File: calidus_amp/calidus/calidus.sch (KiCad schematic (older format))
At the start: 0 parts

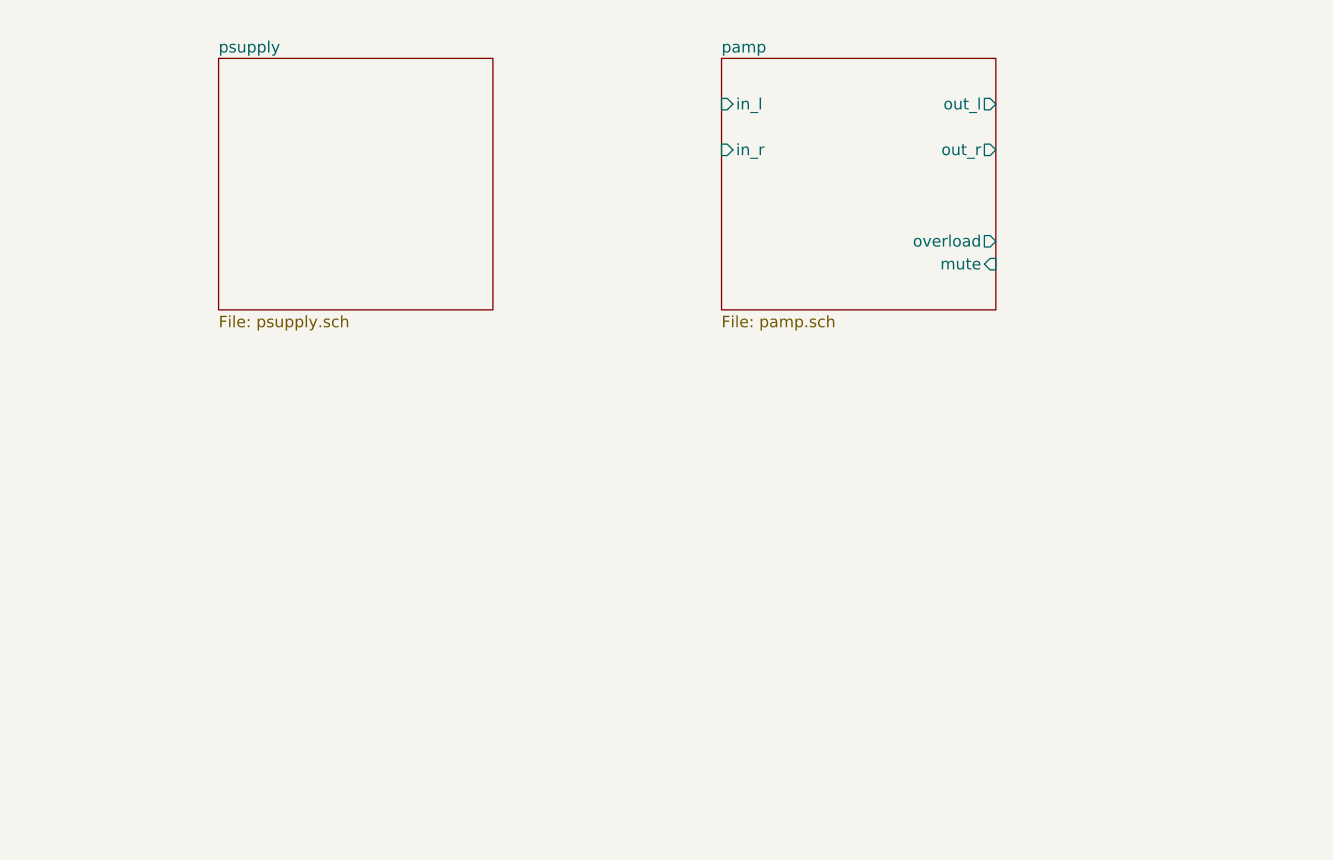
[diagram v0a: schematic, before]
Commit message: Update of the schematic
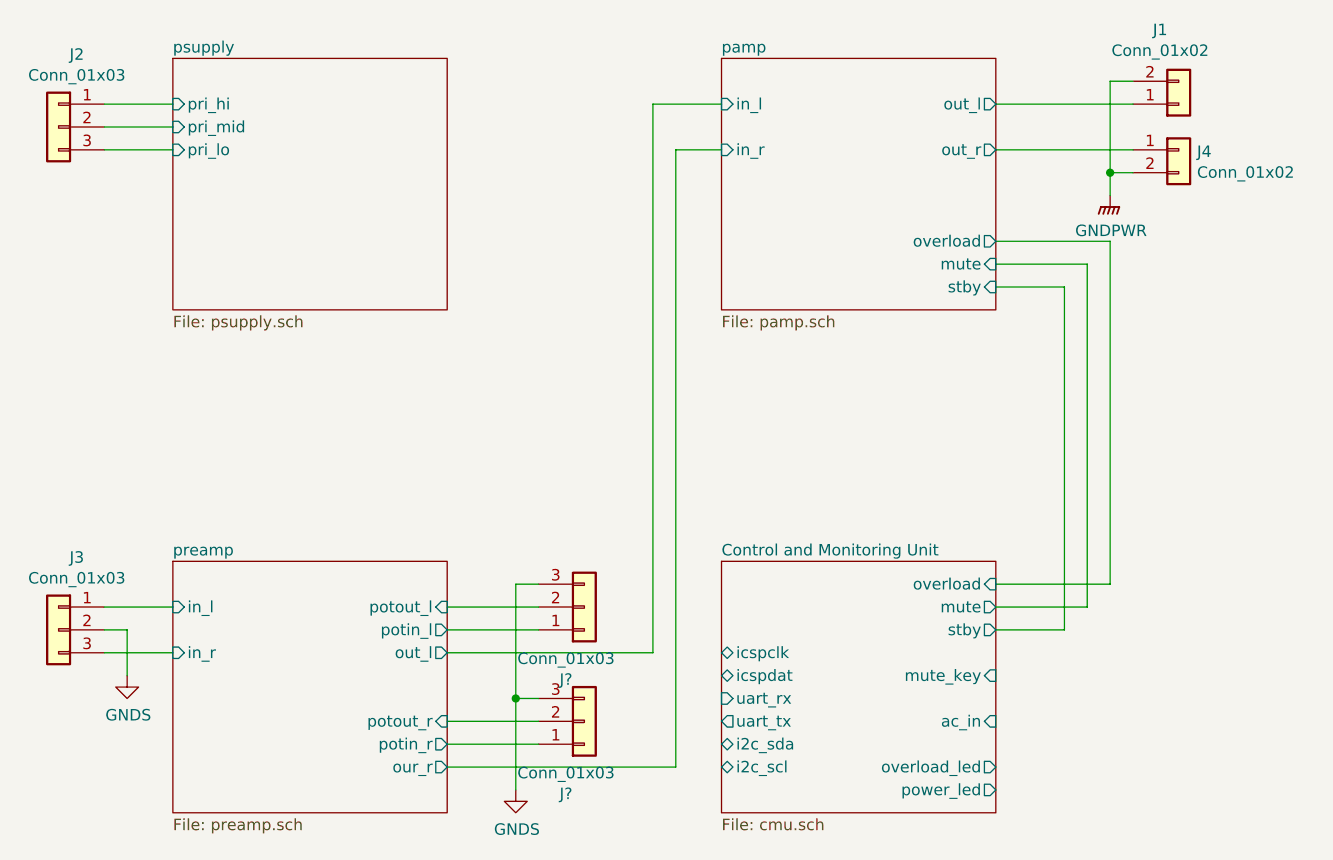
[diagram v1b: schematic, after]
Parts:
- added J1, J4: Conn_01x02, symbol Connector_Generic:Conn_01x02
- added J2, J3, J? (x2): Conn_01x03, symbol Connector_Generic:Conn_01x03
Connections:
- net pamp/out_l: now also J1.1 (Pin_1)
- net pamp/out_r: now also J4.1 (Pin_1)
- new net GNDPWR: J1.2 (Pin_2), J4.2 (Pin_2)
- new net GNDS: J3.2 (Pin_2), J?.3 (Pin_3), J?.3 (Pin_3)
- new net preamp/in_l: J3.1 (Pin_1)
- new net preamp/in_r: J3.3 (Pin_3)
- new net preamp/potin_l: J?.1 (Pin_1)
- new net preamp/potin_r: J?.1 (Pin_1)
- new net preamp/potout_l: J?.2 (Pin_2)
- new net preamp/potout_r: J?.2 (Pin_2)
- new net psupply/pri_hi: J2.1 (Pin_1)
- new net psupply/pri_lo: J2.3 (Pin_3)
- new net psupply/pri_mid: J2.2 (Pin_2)
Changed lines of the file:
@@
 $Descr A4 11693 8268
 encoding utf-8
-Sheet 1 3
+Sheet 1 5
 Title ""
 Date ""
@@
 $EndDescr
 $Sheet
-S 2100 1600 1200 1100
+S 1900 1600 1200 1100
 U 5C37BC48
 F0 "psupply" 50
 F1 "psupply.sch" 50
+F2 "pri_hi" I L 1900 1800 50
+F3 "pri_mid" I L 1900 1900 50
+F4 "pri_lo" I L 1900 2000 50
 $EndSheet
 $Sheet
@@
 F6 "in_r" I L 4300 2000 50
 F7 "out_r" O R 5500 2000 50
-$EndSheet
+F8 "stby" I R 5500 2600 50
+$EndSheet
+$Comp
+L Connector_Generic:Conn_01x03 J2
+U 1 1 5C47FAB8
+P 1400 1900
+F 0 "J2" H 1320 2217 50  0000 C CNN
+F 1 "Conn_01x03" H 1320 2126 50  0000 C CNN
+F 2 "" H 1400 1900 50  0001 C CNN
+F 3 "~" H 1400 1900 50  0001 C CNN
+	1    1400 1900
+	-1   0    0    -1
+$EndComp
+Wire Wire Line
+	1600 1800 1900 1800
+Wire Wire Line
+	1600 1900 1900 1900
+Wire Wire Line
+	1600 2000 1900 2000
+$Comp
+L Connector_Generic:Conn_01x03 J3
+U 1 1 5C47FB17
+P 1400 4100
+F 0 "J3" H 1320 4417 50  0000 C CNN
+F 1 "Conn_01x03" H 1320 4326 50  0000 C CNN
+F 2 "" H 1400 4100 50  0001 C CNN
+F 3 "~" H 1400 4100 50  0001 C CNN
+	1    1400 4100
+	-1   0    0    -1
+$EndComp
+$Comp
+L power:GNDS #PWR01
+U 1 1 5C47FB54
+P 1700 4300
+F 0 "#PWR01" H 1700 4050 50  0001 C CNN
+F 1 "GNDS" H 1705 4127 50  0000 C CNN
+F 2 "" H 1700 4300 50  0001 C CNN
+F 3 "" H 1700 4300 50  0001 C CNN
+	1    1700 4300
+	1    0    0    -1
+$EndComp
+Wire Wire Line
+	1700 4300 1700 4100
+Wire Wire Line
+	1700 4100 1600 4100
+Wire Wire Line
+	1600 4000 1900 4000
+Wire Wire Line
+	1600 4200 1900 4200
+$Comp
+L Connector_Generic:Conn_01x02 J1
+U 1 1 5C47FBF8
+P 6300 1800
+F 0 "J1" H 6219 1475 50  0000 C CNN
+F 1 "Conn_01x02" H 6219 1566 50  0000 C CNN
+F 2 "" H 6300 1800 50  0001 C CNN
+F 3 "~" H 6300 1800 50  0001 C CNN
+	1    6300 1800
+	1    0    0    1
+$EndComp
+$Comp
+L Connector_Generic:Conn_01x02 J4
+U 1 1 5C47FC30
+P 6300 2000
+F 0 "J4" H 6380 1992 50  0000 L CNN
+F 1 "Conn_01x02" H 6380 1901 50  0000 L CNN
+F 2 "" H 6300 2000 50  0001 C CNN
+F 3 "~" H 6300 2000 50  0001 C CNN
+	1    6300 2000
+	1    0    0    -1
+$EndComp
+Wire Wire Line
+	5500 1800 6100 1800
+Wire Wire Line
+	5500 2000 6100 2000
+Wire Wire Line
+	6100 1700 6000 1700
+Wire Wire Line
+	6000 1700 6000 2100
+Wire Wire Line
+	6000 2100 6100 2100
+$Comp
+L power:GNDPWR #PWR02
+U 1 1 5C47FEE1
+P 6000 2200
+F 0 "#PWR02" H 6000 2000 50  0001 C CNN
+F 1 "GNDPWR" H 6004 2046 50  0000 C CNN
+F 2 "" H 6000 2150 50  0001 C CNN
+F 3 "" H 6000 2150 50  0001 C CNN
+	1    6000 2200
+	1    0    0    -1
+$EndComp
+Wire Wire Line
+	6000 2200 6000 2100
+Connection ~ 6000 2100
+$Sheet
+S 1900 3800 1200 1100
+U 5C4751C0
+F0 "preamp" 50
+F1 "preamp.sch" 50
+F2 "potout_l" I R 3100 4000 50
+F3 "potin_l" O R 3100 4100 50
+F4 "out_l" O R 3100 4200 50
+F5 "in_l" I L 1900 4000 50
+F6 "in_r" I L 1900 4200 50
+F7 "potin_r" O R 3100 4600 50
+F8 "potout_r" I R 3100 4500 50
+F9 "our_r" O R 3100 4700 50
+$EndSheet
+Wire Wire Line
+	3100 4200 4000 4200
+Wire Wire Line
+	4000 4200 4000 1800
+Wire Wire Line
+	4000 1800 4300 1800
+Wire Wire Line
+	3100 4700 4100 4700
+Wire Wire Line
+	4100 4700 4100 2000
+Wire Wire Line
+	4100 2000 4300 2000
+$Comp
+L Connector_Generic:Conn_01x03 J?
+U 1 1 5C438B71
+P 3700 4000
+F 0 "J?" H 3620 4317 50  0000 C CNN
+F 1 "Conn_01x03" H 3620 4226 50  0000 C CNN
+F 2 "" H 3700 4000 50  0001 C CNN
+F 3 "~" H 3700 4000 50  0001 C CNN
+	1    3700 4000
+	1    0    0    1
+$EndComp
+Wire Wire Line
+	3100 4100 3500 4100
+Wire Wire Line
+	3500 4000 3100 4000
+$Comp
+L Connector_Generic:Conn_01x03 J?
+U 1 1 5C4396C1
+P 3700 4500
+F 0 "J?" H 3620 4817 50  0000 C CNN
+F 1 "Conn_01x03" H 3620 4726 50  0000 C CNN
+F 2 "" H 3700 4500 50  0001 C CNN
+F 3 "~" H 3700 4500 50  0001 C CNN
+	1    3700 4500
+	1    0    0    1
+$EndComp
+Wire Wire Line
+	3500 4600 3100 4600
+Wire Wire Line
+	3100 4500 3500 4500
+Wire Wire Line
+	3400 4800 3400 4400
+Wire Wire Line
+	3400 4400 3500 4400
+Wire Wire Line
+	3400 4400 3400 3900
+Wire Wire Line
+	3400 3900 3500 3900
+Connection ~ 3400 4400
+$Comp
+L power:GNDS #PWR?
+U 1 1 5C43A2D2
+P 3400 4800
+F 0 "#PWR?" H 3400 4550 50  0001 C CNN
+F 1 "GNDS" H 3405 4627 50  0000 C CNN
+F 2 "" H 3400 4800 50  0001 C CNN
+F 3 "" H 3400 4800 50  0001 C CNN
+	1    3400 4800
+	1    0    0    -1
+$EndComp
+$Sheet
+S 4300 3800 1200 1100
+U 5C43C4AB
+F0 "Control and Monitoring Unit" 50
+F1 "cmu.sch" 50
+F2 "mute" O R 5500 4000 50
+F3 "stby" O R 5500 4100 50
+F4 "power_led" O R 5500 4800 50
+F5 "overload_led" O R 5500 4700 50
+F6 "overload" I R 5500 3900 50
+F7 "ac_in" I R 5500 4500 50
+F8 "mute_key" I R 5500 4300 50
+F9 "icspclk" B L 4300 4200 50
+F10 "icspdat" B L 4300 4300 50
+F11 "uart_rx" I L 4300 4400 50
+F12 "uart_tx" O L 4300 4500 50
+F13 "i2c_sda" B L 4300 4600 50
+F14 "i2c_scl" B L 4300 4700 50
+$EndSheet
+Wire Wire Line
+	5500 2600 5800 2600
+Wire Wire Line
+	5800 2600 5800 4100
+Wire Wire Line
+	5800 4100 5500 4100
+Wire Wire Line
+	5500 4000 5900 4000
+Wire Wire Line
+	5900 4000 5900 2500
+Wire Wire Line
+	5900 2500 5500 2500
+Wire Wire Line
+	5500 2400 6000 2400
+Wire Wire Line
+	6000 2400 6000 3900
+Wire Wire Line
+	6000 3900 5500 3900
 $EndSCHEMATC

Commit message: Daily update
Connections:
- net preamp/potout_l is gone; now on net pamp/in_l: J?.2 (Pin_2)
- net preamp/potout_r is gone; now on net pamp/in_r: J?.2 (Pin_2)
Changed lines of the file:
@@
 F2 "potout_l" I R 3100 4000 50
 F3 "potin_l" O R 3100 4100 50
-F4 "out_l" O R 3100 4200 50
 F5 "in_l" I L 1900 4000 50
 F6 "in_r" I L 1900 4200 50
 F7 "potin_r" O R 3100 4600 50
 F8 "potout_r" I R 3100 4500 50
-F9 "our_r" O R 3100 4700 50
 $EndSheet
 Wire Wire Line
-	3100 4200 4000 4200
+	3200 3600 4000 3600
 Wire Wire Line
-	4000 4200 4000 1800
+	4000 3600 4000 1800
 Wire Wire Line
 	4000 1800 4300 1800
 Wire Wire Line
-	3100 4700 4100 4700
+	3300 3700 4100 3700
 Wire Wire Line
-	4100 4700 4100 2000
+	4100 3700 4100 2000
 Wire Wire Line
 	4100 2000 4300 2000
@@
 	3100 4100 3500 4100
 Wire Wire Line
-	3500 4000 3100 4000
+	3500 4000 3200 4000
 $Comp
 L Connector_Generic:Conn_01x03 J?
@@
 	3500 4600 3100 4600
 Wire Wire Line
-	3100 4500 3500 4500
+	3100 4500 3300 4500
 Wire Wire Line
 	3400 4800 3400 4400
@@
 Wire Wire Line
 	6000 3900 5500 3900
+Wire Wire Line
+	3200 3600 3200 4000
+Connection ~ 3200 4000
+Wire Wire Line
+	3200 4000 3100 4000
+Wire Wire Line
+	3300 3700 3300 4500
+Connection ~ 3300 4500
+Wire Wire Line
+	3300 4500 3500 4500
 $EndSCHEMATC

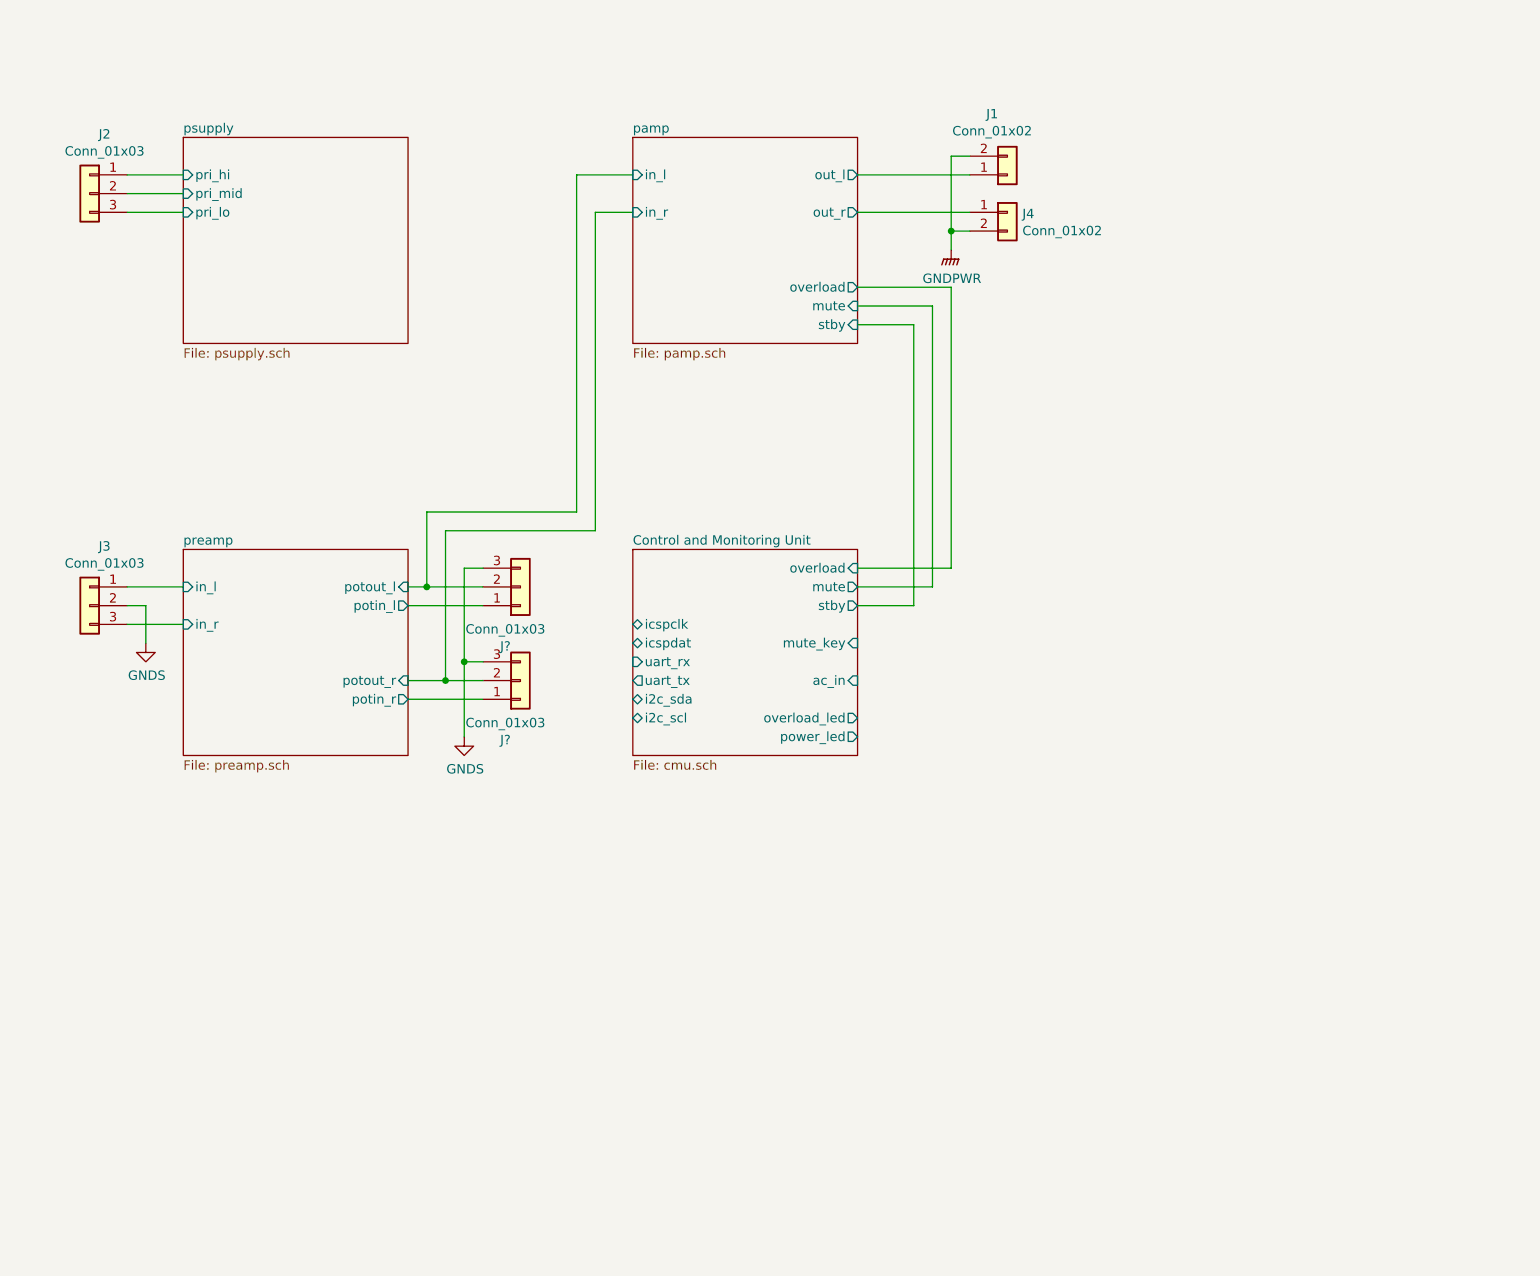
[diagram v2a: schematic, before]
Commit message: Updated component designators and finished CMU
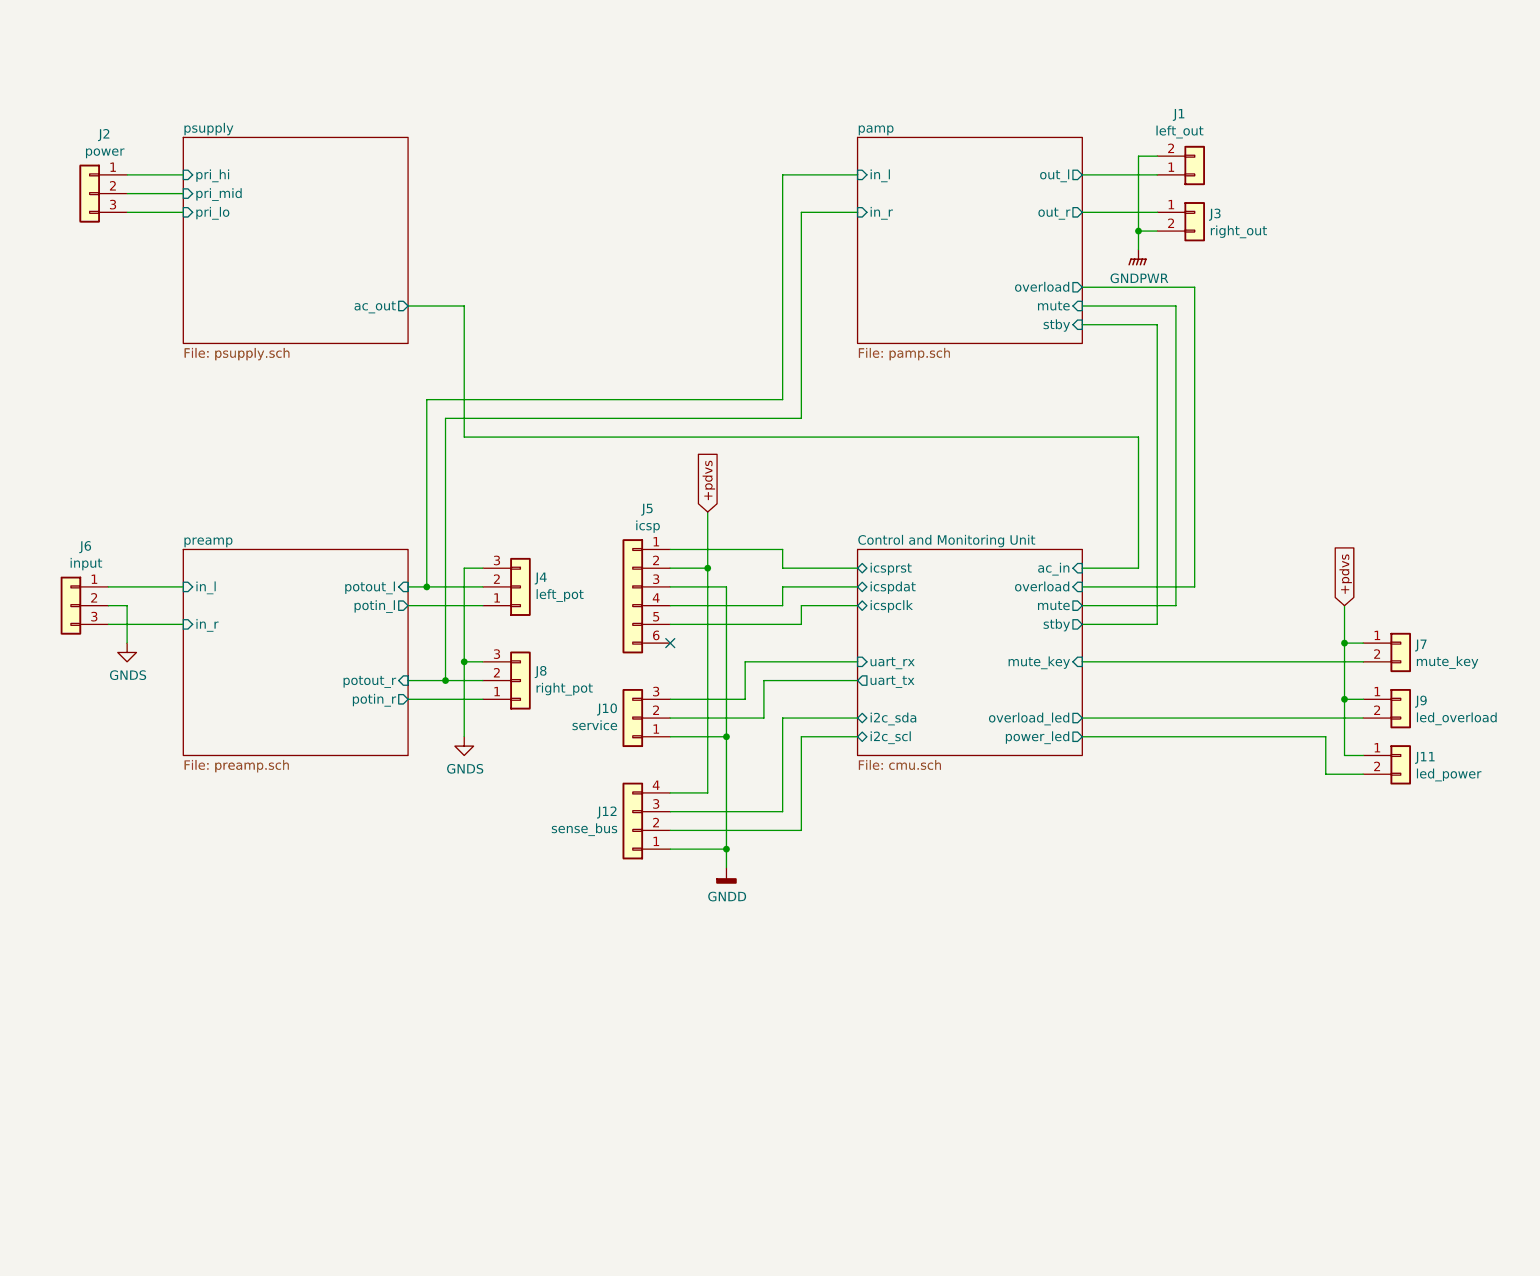
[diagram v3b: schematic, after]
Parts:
- added J10: service, Connector_PinHeader_2.54mm:PinHeader_1x03_P2.54mm_Vertical, symbol Connector_Generic:Conn_01x03
- added J11: led_power, Connector_PinHeader_2.54mm:PinHeader_1x02_P2.54mm_Vertical, symbol Connector_Generic:Conn_01x02
- added J12: sense_bus, Connector_PinHeader_2.54mm:PinHeader_1x04_P2.54mm_Vertical, symbol Connector_Generic:Conn_01x04
- added J5: icsp, Connector_PinHeader_2.54mm:PinHeader_1x06_P2.54mm_Vertical, symbol Connector_Generic:Conn_01x06
- added J7: mute_key, Connector_PinHeader_2.54mm:PinHeader_1x02_P2.54mm_Vertical, symbol Connector_Generic:Conn_01x02
- added J9: led_overload, Connector_PinHeader_2.54mm:PinHeader_1x02_P2.54mm_Vertical, symbol Connector_Generic:Conn_01x02
- J1: value Conn_01x02 -> left_out
- J2: value Conn_01x03 -> power
- J3: renamed from J4; value Conn_01x02 -> right_out
- J4: renamed from J?; value Conn_01x03 -> left_pot
- J6: renamed from J3; value Conn_01x03 -> input
- J8: renamed from J?; value Conn_01x03 -> right_pot
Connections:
- net Control and Monitoring Unit/i2c_scl: now also J12.2 (Pin_2)
- net Control and Monitoring Unit/i2c_sda: now also J12.3 (Pin_3)
- net Control and Monitoring Unit/icspclk: now also J5.5 (Pin_5)
- net Control and Monitoring Unit/icspdat: now also J5.4 (Pin_4)
- net Control and Monitoring Unit/mute_key: now also J7.2 (Pin_2)
- net Control and Monitoring Unit/overload_led: now also J9.2 (Pin_2)
- net Control and Monitoring Unit/power_led: now also J11.2 (Pin_2)
- net Control and Monitoring Unit/uart_rx: now also J10.3 (Pin_3)
- net Control and Monitoring Unit/uart_tx: now also J10.2 (Pin_2)
- new net +pdvs: J11.1 (Pin_1), J12.4 (Pin_4), J5.2 (Pin_2), J7.1 (Pin_1), J9.1 (Pin_1)
- new net Control and Monitoring Unit/icsprst: J5.1 (Pin_1)
- new net GNDD: J10.1 (Pin_1), J12.1 (Pin_1), J5.3 (Pin_3)
- no-connect marks 0 -> 1
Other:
- moved on the sheet: J1, J3, J6
